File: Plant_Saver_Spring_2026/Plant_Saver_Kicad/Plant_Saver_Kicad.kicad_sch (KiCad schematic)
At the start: 22 parts, among them SW1 Up, SW2 Down, SW3 Change Screen, SW4 Select, SW5 Select, SW7 Select, U14 CDBA140SL-HF, U18 ESP32-WROOM-32E-N16, U3 ESP32-WROOM-32D, U5 CDBA140SL-HF, U6 CDBA140SL-HF, U7 CDBA140SL-HF

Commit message: Footprint correction
Changed the DHT20 from a header pin to the recommended SIP. Also had to reannotate in order to assign footprints.
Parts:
- U1: renamed from U5; footprint CDBA-HF -> (none)
- U2: renamed from U6; footprint CDBA-HF -> (none)
- U3: renamed from U14; footprint CDBA-HF -> (none)
- U4: renamed from U7; footprint CDBA-HF -> (none)
- U6: renamed from U2; footprint Connector_PinHeader_2.54mm:PinHeader_1x04_P2.54mm_Vertical -> Resistor_THT:R_Array_SIP4
- renumbered C7 to C1, C13 to C2, R37 to R1, SW7 to SW1, SW5 to SW2, SW1 to SW3, SW2 to SW4, SW3 to SW5, SW4 to SW6, U18 to U5, U4 to U7, U3 to U8, U13 to U9
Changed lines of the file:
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@@
 		(dnp no)
 		(fields_autoplaced yes)
-		(property "Reference" "#PWR026"
+		(property "Reference" "#PWR07"
 			(at 215.9 173.99 0)
 			(effects
@@
 			(project "Plant_Saver_Kicad"
 				(path "/7f244634-d37a-4ff0-ba36-8027330ab1bd"
-					(reference "#PWR026")
+					(reference "#PWR07")
 					(unit 1)
 				)
@@
 		(on_board yes)
 		(dnp no)
-		(property "Reference" "#PWR06"
+		(property "Reference" "#PWR08"
 			(at 259.08 158.75 0)
 			(effects
@@
 			(project "Plant_Saver_Kicad"
 				(path "/7f244634-d37a-4ff0-ba36-8027330ab1bd"
-					(reference "#PWR06")
+					(reference "#PWR08")
 					(unit 1)
 				)
@@
 		(dnp no)
 		(fields_autoplaced yes)
-		(property "Reference" "U18"
+		(property "Reference" "U5"
 			(at 243.84 175.26 0)
 			(effects
@@
 			(project ""
 				(path "/7f244634-d37a-4ff0-ba36-8027330ab1bd"
-					(reference "U18")
+					(reference "U5")
 					(unit 1)
 				)
@@
 		(dnp no)
 		(fields_autoplaced yes)
-		(property "Reference" "SW3"
+		(property "Reference" "SW5"
 			(at 368.3 152.4 0)
 			(effects
@@
 			(project "Plant_Saver_Kicad"
 				(path "/7f244634-d37a-4ff0-ba36-8027330ab1bd"
-					(reference "SW3")
+					(reference "SW5")
 					(unit 1)
 				)
@@
 		(on_board yes)
 		(dnp no)
-		(property "Reference" "C13"
+		(property "Reference" "C2"
 			(at 185.42 198.882 0)
 			(effects
@@
 			(project "Plant_Saver_Kicad"
 				(path "/7f244634-d37a-4ff0-ba36-8027330ab1bd"
-					(reference "C13")
+					(reference "C2")
 					(unit 1)
 				)
@@
 		(on_board yes)
 		(dnp no)
-		(property "Reference" "#PWR011"
+		(property "Reference" "#PWR010"
 			(at 308.61 160.02 0)
 			(effects
@@
 			(project "Plant_Saver_Kicad"
 				(path "/7f244634-d37a-4ff0-ba36-8027330ab1bd"
-					(reference "#PWR011")
+					(reference "#PWR010")
 					(unit 1)
 				)
@@
 		(dnp no)
 		(fields_autoplaced yes)
-		(property "Reference" "U5"
+		(property "Reference" "U1"
 			(at 31.75 143.5099 90)
 			(effects
@@
 			)
 		)
-		(property "Footprint" "CDBA-HF"
+		(property "Footprint" ""
 			(at 27.94 139.7 0)
 			(effects
@@
 			(project ""
 				(path "/7f244634-d37a-4ff0-ba36-8027330ab1bd"
-					(reference "U5")
+					(reference "U1")
 					(unit 1)
 				)
@@
 		(dnp no)
 		(fields_autoplaced yes)
-		(property "Reference" "#PWR024"
+		(property "Reference" "#PWR05"
 			(at 165.1 205.74 0)
 			(effects
@@
 			(project "Plant_Saver_Kicad"
 				(path "/7f244634-d37a-4ff0-ba36-8027330ab1bd"
-					(reference "#PWR024")
+					(reference "#PWR05")
 					(unit 1)
 				)
@@
 		(on_board yes)
 		(dnp no)
-		(property "Reference" "C7"
+		(property "Reference" "C1"
 			(at 168.402 190.5 0)
 			(effects
@@
 			(project "Plant_Saver_Kicad"
 				(path "/7f244634-d37a-4ff0-ba36-8027330ab1bd"
-					(reference "C7")
+					(reference "C1")
 					(unit 1)
 				)
@@
 		(dnp no)
 		(fields_autoplaced yes)
-		(property "Reference" "#PWR01"
+		(property "Reference" "#PWR02"
 			(at 33.02 124.46 0)
 			(effects
@@
 			(project ""
 				(path "/7f244634-d37a-4ff0-ba36-8027330ab1bd"
-					(reference "#PWR01")
+					(reference "#PWR02")
 					(unit 1)
 				)
@@
 		(dnp no)
 		(fields_autoplaced yes)
-		(property "Reference" "SW5"
+		(property "Reference" "SW2"
 			(at 278.13 233.68 0)
 			(effects
@@
 			(project "Plant_Saver_Kicad"
 				(path "/7f244634-d37a-4ff0-ba36-8027330ab1bd"
-					(reference "SW5")
+					(reference "SW2")
 					(unit 1)
 				)
@@
 		(on_board yes)
 		(dnp no)
-		(property "Reference" "U3"
+		(property "Reference" "U8"
 			(at 295.656 176.53 0)
 			(effects
@@
 			(project "Plant_Saver_Kicad"
 				(path "/7f244634-d37a-4ff0-ba36-8027330ab1bd"
-					(reference "U3")
+					(reference "U8")
 					(unit 1)
 				)
@@
 		(dnp no)
 		(fields_autoplaced yes)
-		(property "Reference" "U14"
+		(property "Reference" "U3"
 			(at 87.63 143.5099 90)
 			(effects
@@
 			)
 		)
-		(property "Footprint" "CDBA-HF"
+		(property "Footprint" ""
 			(at 83.82 139.7 0)
 			(effects
@@
 			(project "Plant_Saver_Kicad"
 				(path "/7f244634-d37a-4ff0-ba36-8027330ab1bd"
-					(reference "U14")
+					(reference "U3")
 					(unit 1)
 				)
@@
 		(dnp no)
 		(fields_autoplaced yes)
-		(property "Reference" "#PWR025"
+		(property "Reference" "#PWR06"
 			(at 175.26 204.47 0)
 			(effects
@@
 			(project "Plant_Saver_Kicad"
 				(path "/7f244634-d37a-4ff0-ba36-8027330ab1bd"
-					(reference "#PWR025")
+					(reference "#PWR06")
 					(unit 1)
 				)
@@
 		(dnp no)
 		(fields_autoplaced yes)
-		(property "Reference" "SW4"
+		(property "Reference" "SW6"
 			(at 368.3 165.1 0)
 			(effects
@@
 			(project "Plant_Saver_Kicad"
 				(path "/7f244634-d37a-4ff0-ba36-8027330ab1bd"
-					(reference "SW4")
+					(reference "SW6")
 					(unit 1)
 				)
@@
 		(dnp no)
 		(fields_autoplaced yes)
-		(property "Reference" "U7"
+		(property "Reference" "U4"
 			(at 114.3 143.5099 90)
 			(effects
@@
 			)
 		)
-		(property "Footprint" "CDBA-HF"
+		(property "Footprint" ""
 			(at 110.49 139.7 0)
 			(effects
@@
 			(project "Plant_Saver_Kicad"
 				(path "/7f244634-d37a-4ff0-ba36-8027330ab1bd"
-					(reference "U7")
+					(reference "U4")
 					(unit 1)
 				)
@@
 		(dnp no)
 		(fields_autoplaced yes)
-		(property "Reference" "#PWR02"
+		(property "Reference" "#PWR01"
 			(at 33.02 91.44 0)
 			(effects
@@
 			(project "Plant_Saver_Kicad"
 				(path "/7f244634-d37a-4ff0-ba36-8027330ab1bd"
-					(reference "#PWR02")
+					(reference "#PWR01")
 					(unit 1)
 				)
@@
 		(dnp no)
 		(fields_autoplaced yes)
-		(property "Reference" "SW1"
+		(property "Reference" "SW3"
 			(at 368.3 127 0)
 			(effects
@@
 			(project "Plant_Saver_Kicad"
 				(path "/7f244634-d37a-4ff0-ba36-8027330ab1bd"
-					(reference "SW1")
+					(reference "SW3")
 					(unit 1)
 				)
@@
 		(dnp no)
 		(fields_autoplaced yes)
-		(property "Reference" "U13"
+		(property "Reference" "U9"
 			(at 332.74 129.5399 0)
 			(effects
@@
 			(project "Plant_Saver_Kicad"
 				(path "/7f244634-d37a-4ff0-ba36-8027330ab1bd"
-					(reference "U13")
+					(reference "U9")
 					(unit 1)
 				)
@@
 		(dnp no)
 		(fields_autoplaced yes)
-		(property "Reference" "U2"
+		(property "Reference" "U6"
 			(at 266.7 133.9849 0)
 			(effects
@@
 			)
 		)
-		(property "Footprint" "Connector_PinHeader_2.54mm:PinHeader_1x04_P2.54mm_Vertical"
+		(property "Footprint" "Resistor_THT:R_Array_SIP4"
 			(at 257.81 134.62 0)
 			(effects
@@
 			(project "Plant_Saver_Kicad"
 				(path "/7f244634-d37a-4ff0-ba36-8027330ab1bd"
-					(reference "U2")
+					(reference "U6")
 					(unit 1)
 				)
@@
 		(on_board yes)
 		(dnp no)
-		(property "Reference" "SW7"
+		(property "Reference" "SW1"
 			(at 204.47 183.642 0)
 			(effects
@@
 			(project "Plant_Saver_Kicad"
 				(path "/7f244634-d37a-4ff0-ba36-8027330ab1bd"
-					(reference "SW7")
+					(reference "SW1")
 					(unit 1)
 				)
@@
 		(dnp no)
 		(fields_autoplaced yes)
-		(property "Reference" "SW2"
+		(property "Reference" "SW4"
 			(at 368.3 139.7 0)
 			(effects
@@
 			(project "Plant_Saver_Kicad"
 				(path "/7f244634-d37a-4ff0-ba36-8027330ab1bd"
-					(reference "SW2")
+					(reference "SW4")
 					(unit 1)
 				)
@@
 		(on_board yes)
 		(dnp no)
-		(property "Reference" "#PWR022"
+		(property "Reference" "#PWR011"
 			(at 330.2 161.29 0)
 			(effects
@@
 			(project "Plant_Saver_Kicad"
 				(path "/7f244634-d37a-4ff0-ba36-8027330ab1bd"
-					(reference "#PWR022")
+					(reference "#PWR011")
 					(unit 1)
 				)
@@
 		(dnp no)
 		(fields_autoplaced yes)
-		(property "Reference" "R37"
+		(property "Reference" "R1"
 			(at 181.61 184.15 90)
 			(effects
@@
 			(project "Plant_Saver_Kicad"
 				(path "/7f244634-d37a-4ff0-ba36-8027330ab1bd"
-					(reference "R37")
+					(reference "R1")
 					(unit 1)
 				)
@@
 		(dnp no)
 		(fields_autoplaced yes)
-		(property "Reference" "U6"
+		(property "Reference" "U2"
 			(at 59.69 143.5099 90)
 			(effects
@@
 			)
 		)
-		(property "Footprint" "CDBA-HF"
+		(property "Footprint" ""
 			(at 55.88 139.7 0)
 			(effects
@@
 			(project "Plant_Saver_Kicad"
 				(path "/7f244634-d37a-4ff0-ba36-8027330ab1bd"
-					(reference "U6")
+					(reference "U2")
 					(unit 1)
 				)
@@
 		(dnp no)
 		(fields_autoplaced yes)
-		(property "Reference" "#PWR027"
+		(property "Reference" "#PWR09"
 			(at 285.75 250.19 0)
 			(effects
@@
 			(project "Plant_Saver_Kicad"
 				(path "/7f244634-d37a-4ff0-ba36-8027330ab1bd"
-					(reference "#PWR027")
+					(reference "#PWR09")
 					(unit 1)
 				)
@@
 		(dnp no)
 		(fields_autoplaced yes)
-		(property "Reference" "#PWR05"
+		(property "Reference" "#PWR04"
 			(at 152.4 161.29 0)
 			(effects
@@
 			(project ""
 				(path "/7f244634-d37a-4ff0-ba36-8027330ab1bd"
-					(reference "#PWR05")
+					(reference "#PWR04")
 					(unit 1)
 				)
@@
 		(dnp no)
 		(fields_autoplaced yes)
-		(property "Reference" "U4"
+		(property "Reference" "U7"
 			(at 312.42 131.4449 0)
 			(effects
@@
 			(project "Plant_Saver_Kicad"
 				(path "/7f244634-d37a-4ff0-ba36-8027330ab1bd"
-					(reference "U4")
+					(reference "U7")
 					(unit 1)
 				)
@@
 		(dnp no)
 		(fields_autoplaced yes)
-		(property "Reference" "#PWR04"
+		(property "Reference" "#PWR03"
 			(at 101.6 187.96 0)
 			(effects
@@
 			(project "Plant_Saver_Kicad"
 				(path "/7f244634-d37a-4ff0-ba36-8027330ab1bd"
-					(reference "#PWR04")
-					(unit 1)
-				)
+					(reference "#PWR03")
+					(unit 1)
+				)

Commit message: Charging updates and MicroSD started
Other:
- added sheet MicroSD (MicroSD.kicad_sch)
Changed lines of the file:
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@@
+	)
+	(sheet
+		(at 215.9 76.2)
+		(size 38.1 25.4)
+		(exclude_from_sim no)
+		(in_bom yes)
+		(on_board yes)
+		(dnp no)
+		(fields_autoplaced yes)
+		(stroke
+			(width 0.1524)
+			(type solid)
+		)
+		(fill
+			(color 0 0 0 0.0000)
+		)
+		(property "Sheetname" "MicroSD"
+			(at 215.9 75.4884 0)
+			(effects
+				(font
+					(size 1.27 1.27)
+				)
+				(justify left bottom)
+			)
+		)
+		(property "Sheetfile" "MicroSD.kicad_sch"
+			(at 215.9 102.1846 0)
+			(effects
+				(font
+					(size 1.27 1.27)
+				)
+				(justify left top)
+				(hide yes)
+			)
+		)
+		(instances
+			(project "Plant_Saver_Kicad"
+				(path "/7f244634-d37a-4ff0-ba36-8027330ab1bd"
+					(page "10")
+				)
+			)
+		)
 	)
 	(sheet

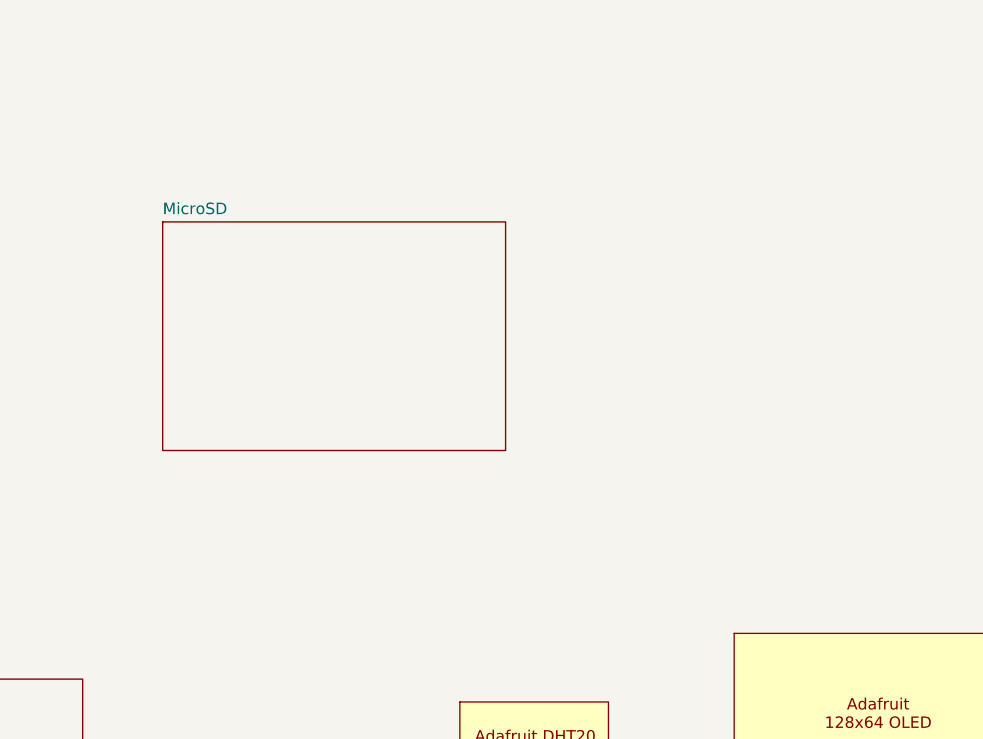
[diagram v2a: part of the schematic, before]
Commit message: Micro-SD subsheet
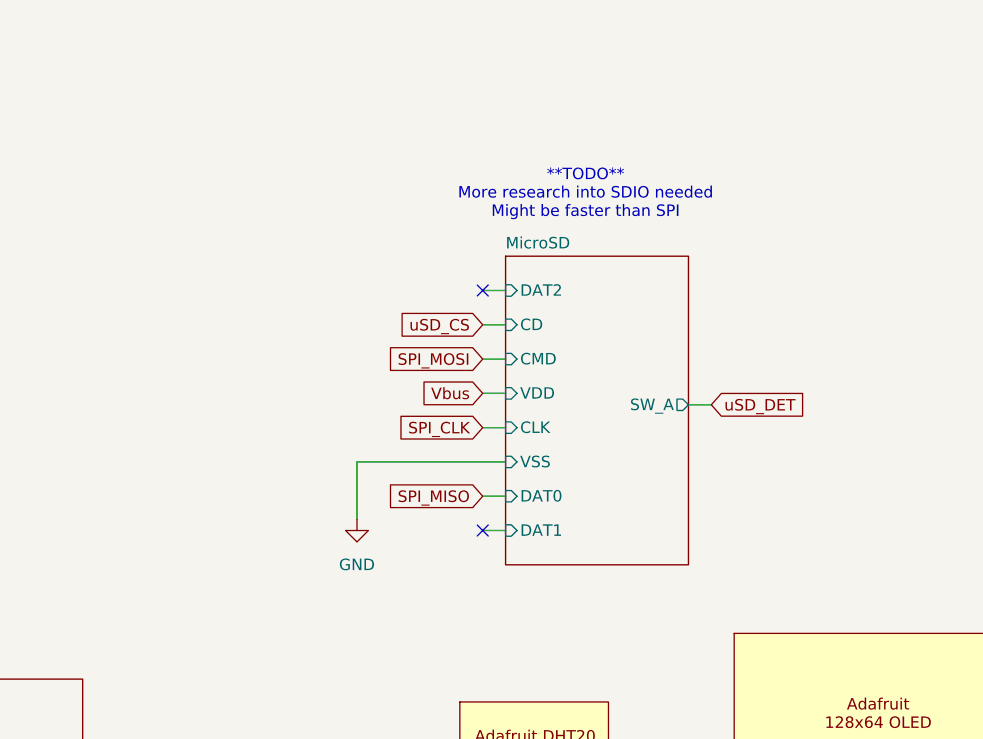
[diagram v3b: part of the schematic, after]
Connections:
- no-connect marks 0 -> 2
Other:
- sheet MicroSD ports: added CD, CLK, CMD, DAT0, DAT1, DAT2, SW_A, VDD, VSS; removed none
- note added: "**TODO** More research into SDIO needed Might be faster than SPI"

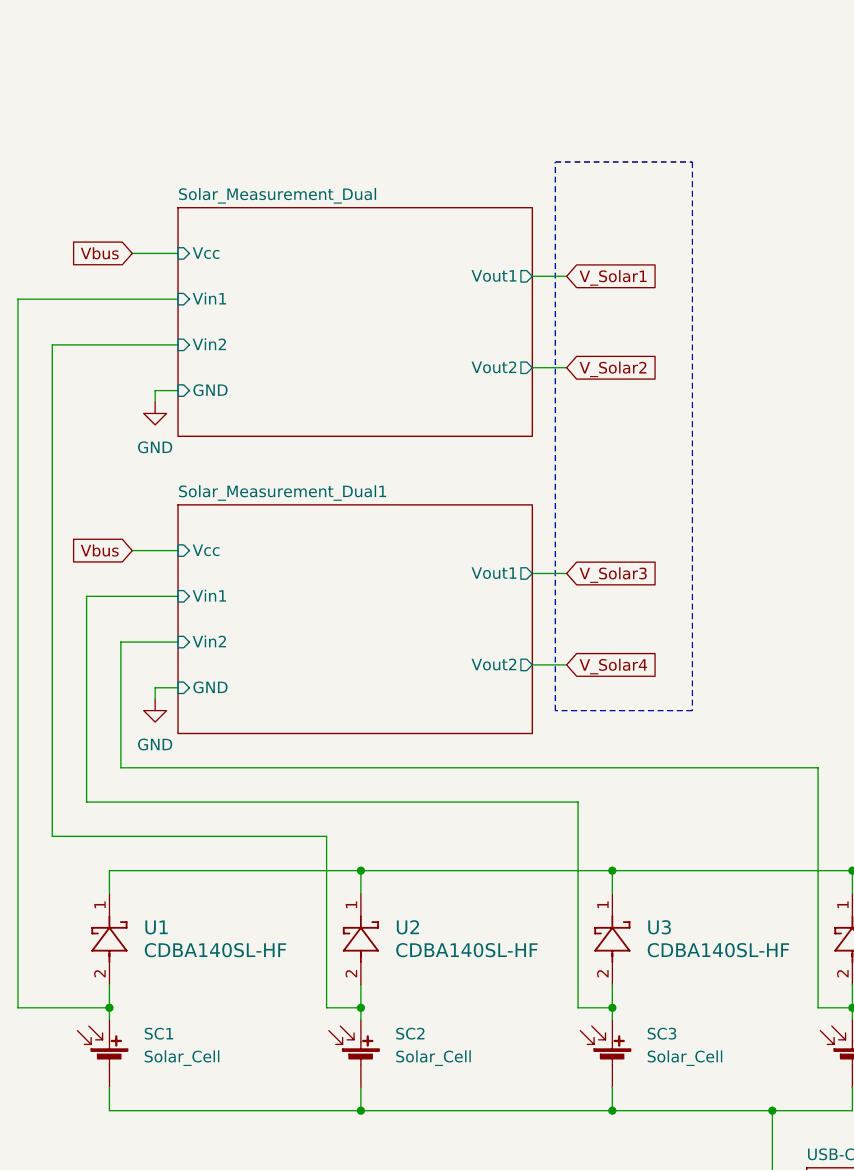
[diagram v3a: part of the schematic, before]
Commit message: Fixed solar measurement circuit
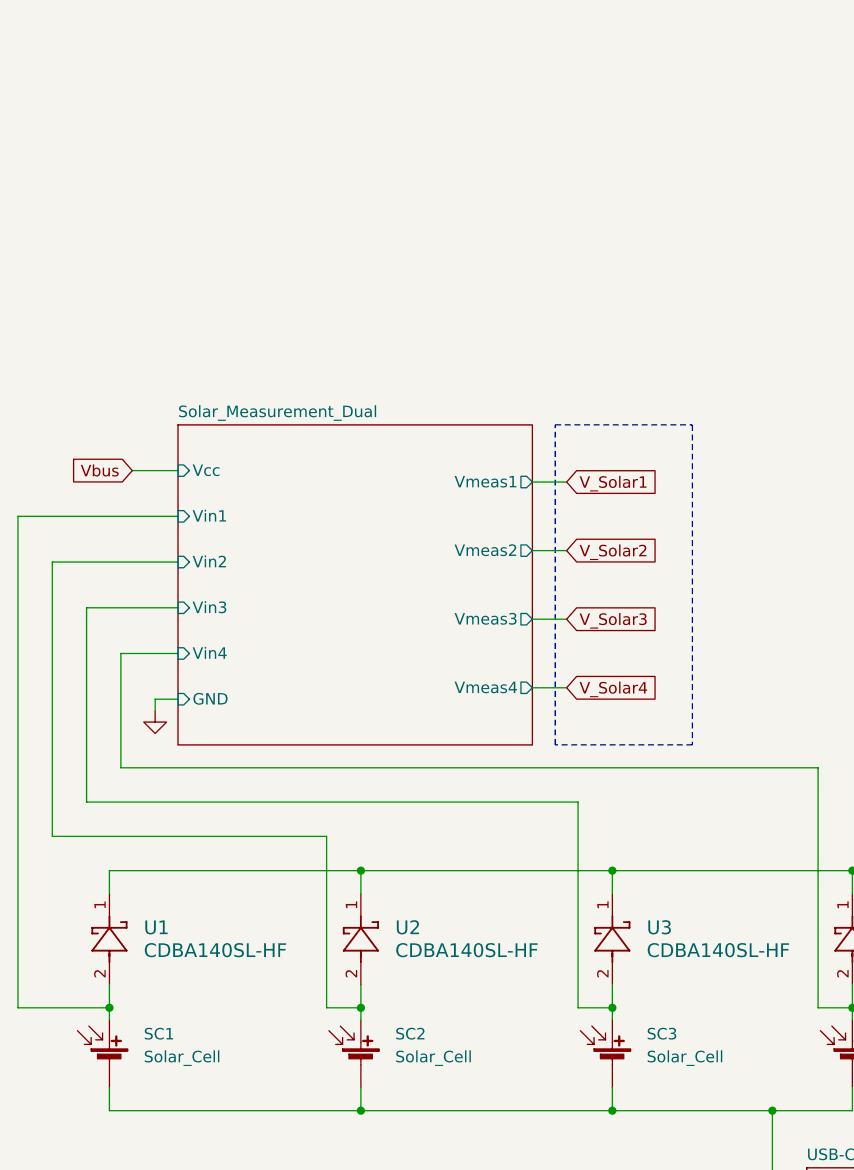
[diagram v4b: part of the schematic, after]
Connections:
- net Solar_Measurement_Dual1/Vin1 renamed Solar_Measurement_Dual/Vin3
- net Solar_Measurement_Dual1/Vin2 renamed Solar_Measurement_Dual/Vin4
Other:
- removed sheet Solar_Measurement_Dual1
- sheet Solar_Measurement_Dual ports: added Vin3, Vin4, Vmeas1, Vmeas2, Vmeas3, Vmeas4; removed Vout1, Vout2

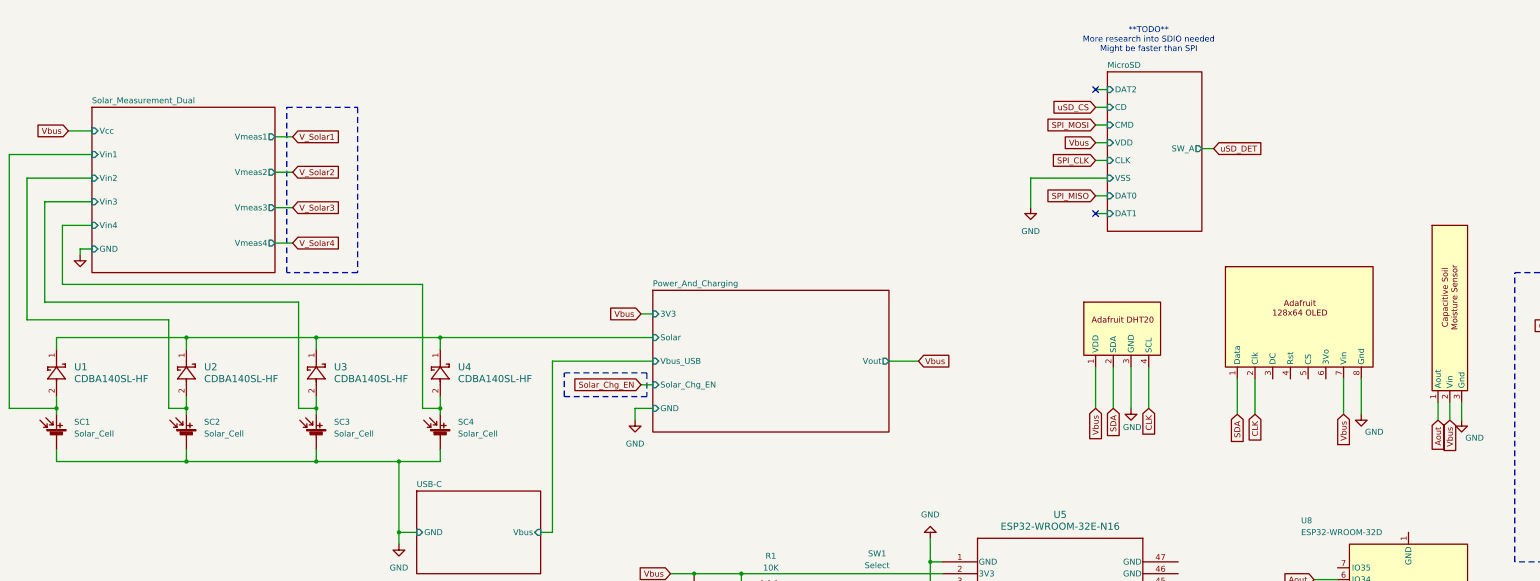
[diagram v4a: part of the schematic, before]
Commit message: Added power switching
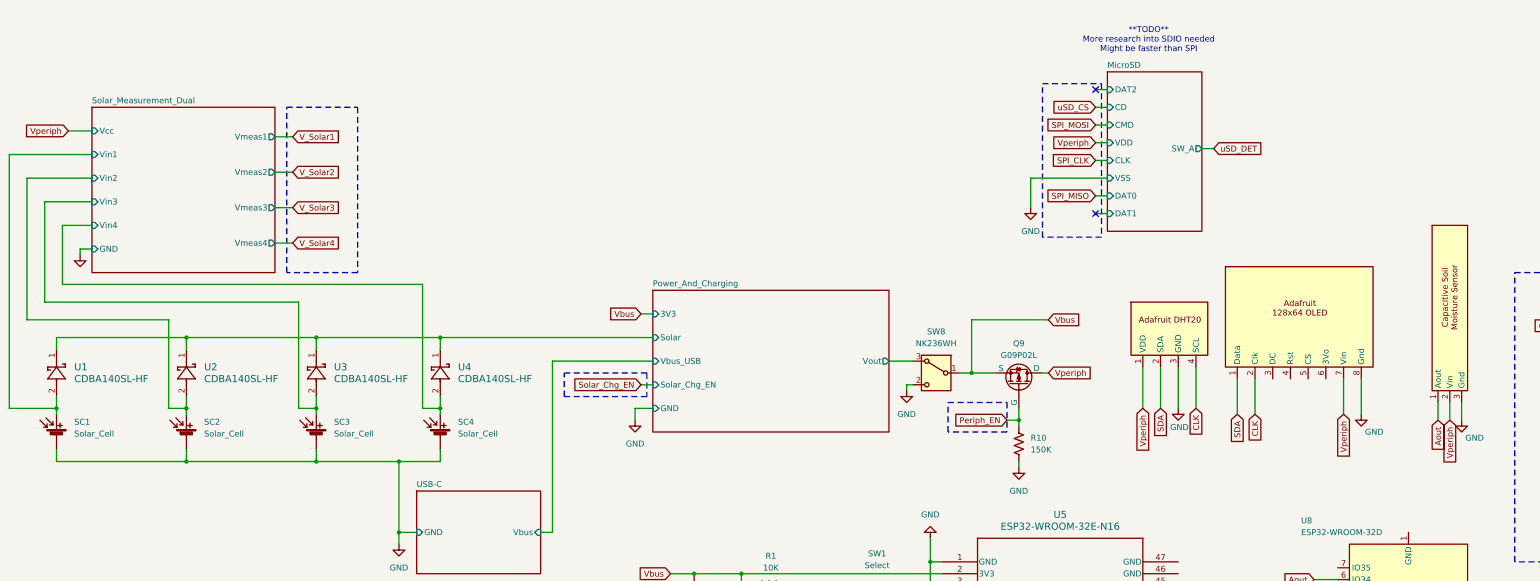
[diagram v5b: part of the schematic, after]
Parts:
- added Q9: G09P02L, G09P02L:TSOT-23, symbol Simulation_SPICE:PMOS
- added R10: 150K, Resistor_THT:R_Axial_DIN0207_L6.3mm_D2.5mm_P10.16mm_Horizontal, symbol Device:R_US
- added SW8: NK236WH, NK236WH:SW_Slide-03_APEM-NK23GWH_10x9.2x2.6_P2.54mm, symbol Switch:SW_Wuerth_450301014042
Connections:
- net GND: now also R10.1, SW8.2 (C)
- net Vbus: now also Q9.3 (S), SW8.1 (B); no longer U6.1 (VDD), U7.7 (Vin), U9.2 (Vin)
- new net Periph_EN: Q9.2 (G), R10.2
- new net Power_And_Charging/Vout: SW8.3 (A)
- new net Vperiph: Q9.1 (D), U6.1 (VDD), U7.7 (Vin), U9.2 (Vin)
